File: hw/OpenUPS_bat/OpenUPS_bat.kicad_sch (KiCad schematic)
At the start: 27 parts, among them Q101 Q_NMOS_GDS, Q102 Q_NMOS_GDS, U102 BQ77915

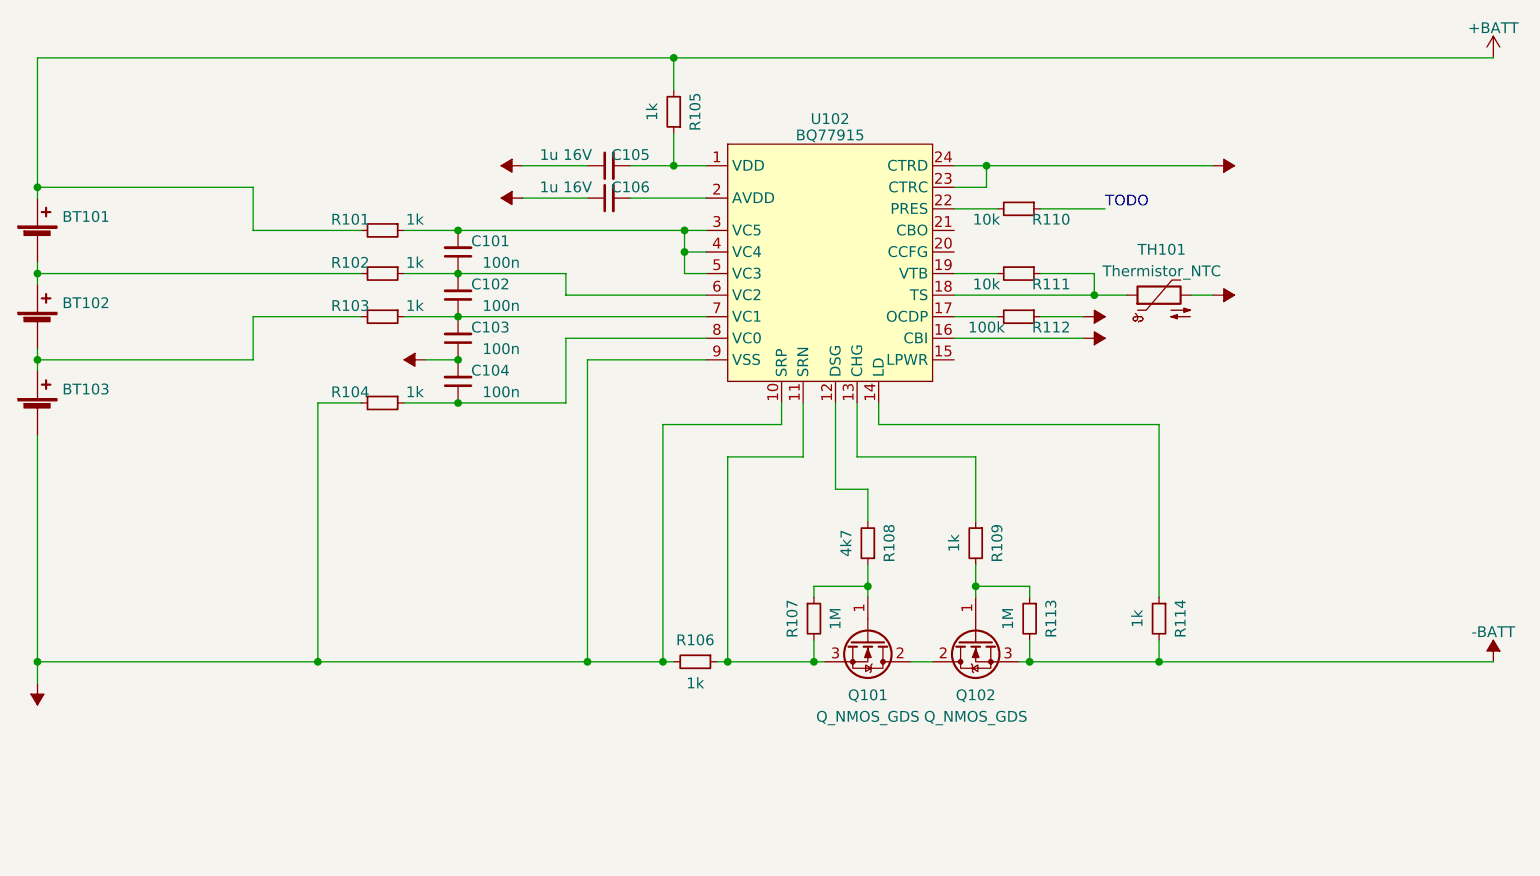
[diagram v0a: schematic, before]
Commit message: Fixed ground symbols
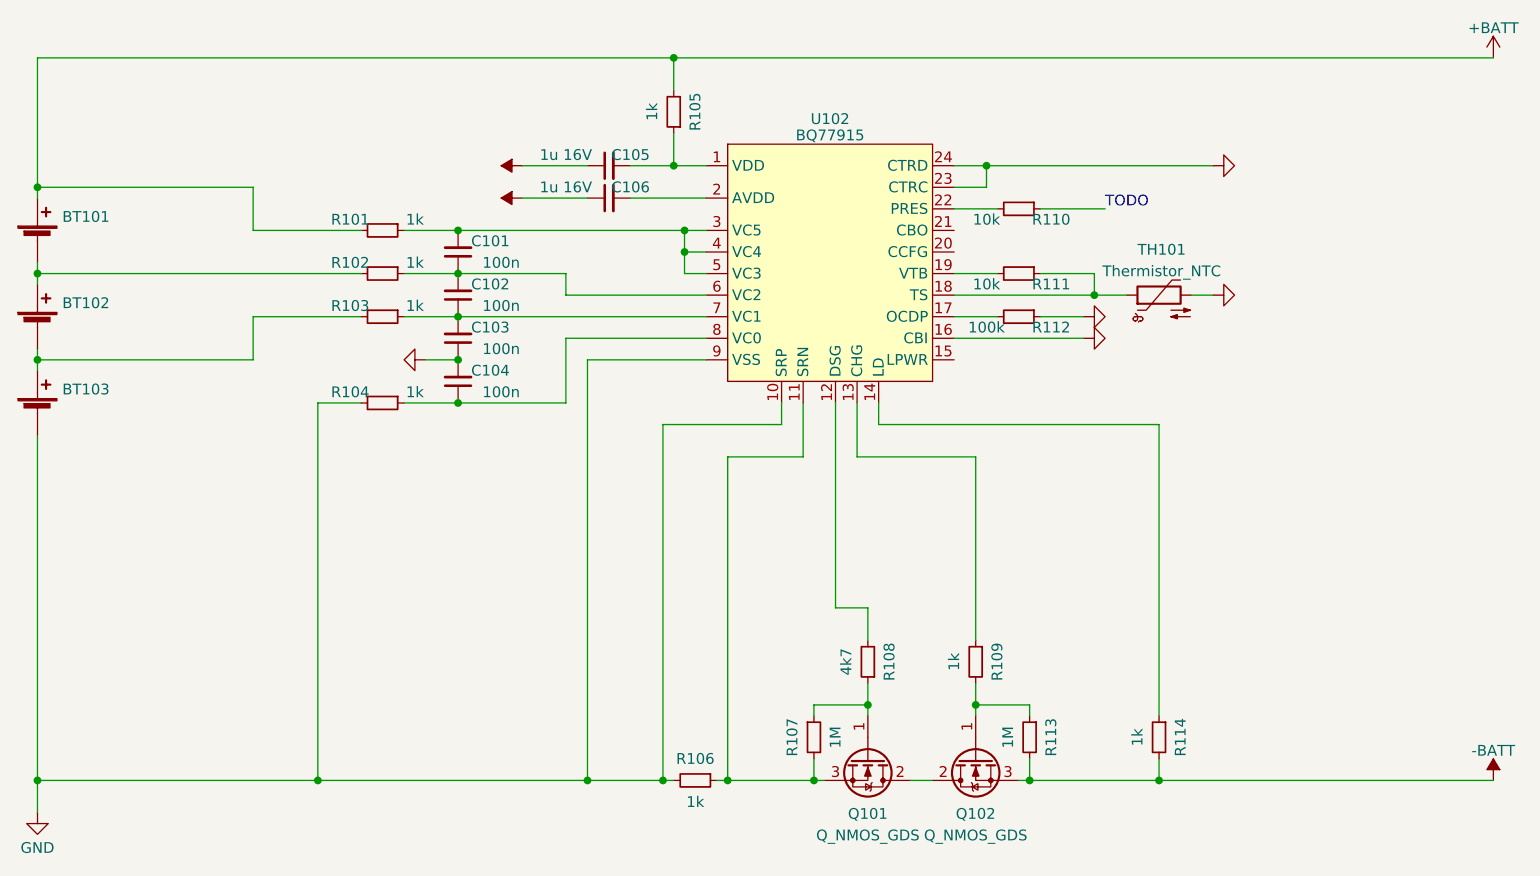
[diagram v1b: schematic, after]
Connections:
- net -BATT: no longer BT103.2 (-), C103.1, C104.2, R104.2, R106.2, R112.1, TH101.2, U102.10 (SRP), U102.16 (CBI), U102.23 (CTRC), U102.24 (CTRD), U102.9 (VSS)
- new net GND: BT103.2 (-), C103.1, C104.2, R104.2, R106.2, R112.1, TH101.2, U102.10 (SRP), U102.16 (CBI), U102.23 (CTRC), U102.24 (CTRD), U102.9 (VSS)
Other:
- moved on the sheet: Q101, Q102, R106, R107, R108, R109, R113, R114
